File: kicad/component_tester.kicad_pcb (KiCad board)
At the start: 2 copper layers, 100.4 x 83 mm, 86 parts, among them IC201 MCP1640, IC202 ATmega328P-MMH, IC301 FT232RL, IC302 MAX1811, J301 0R-JUMPA, J302 0R-JUMPA, Q201 8 MHz, Q401 BSS138, Q402 BSS138, SW201 EVQ, T201 PMV65XP, T202 BSS84, T203 BSS123, T204 BC847, T301 BSS123, U401 VREG_SOT23-5, X201 MICRO-USB, X202 ISP

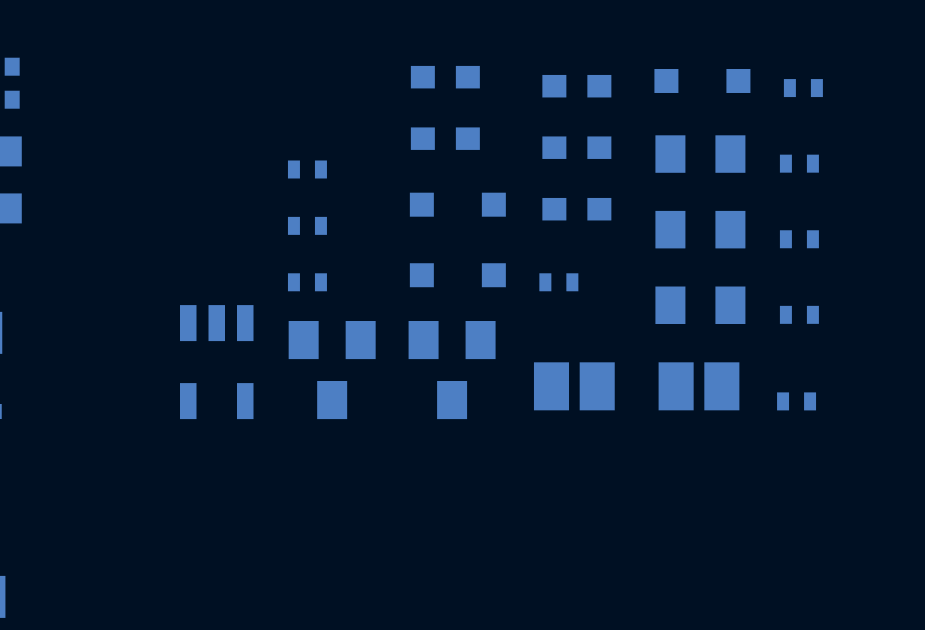
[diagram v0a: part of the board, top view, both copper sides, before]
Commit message: Remove unnecessary stuff from OLED circuitry
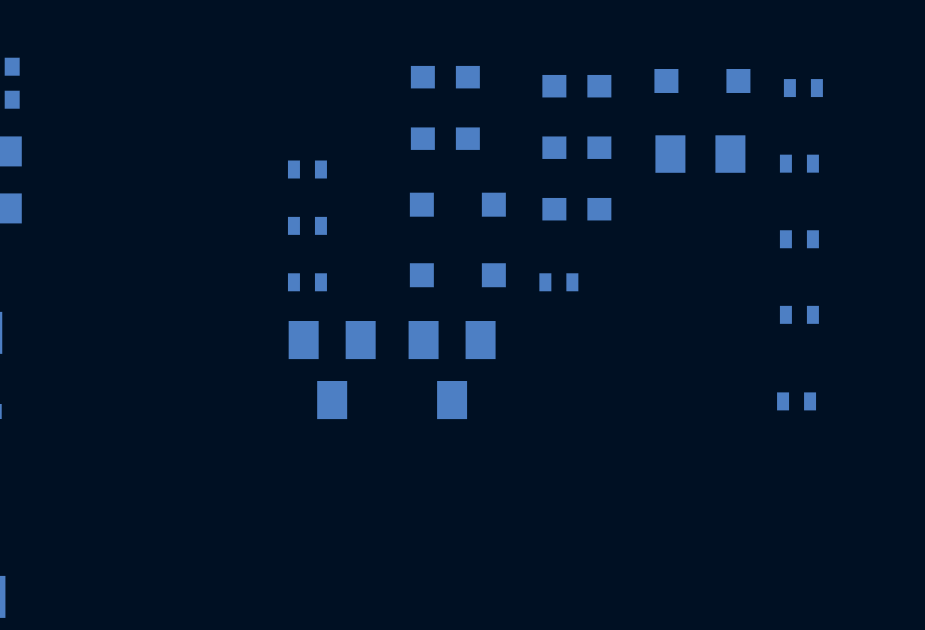
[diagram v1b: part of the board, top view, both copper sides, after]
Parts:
- removed C401, C402: 10uF, KiCad/Capacitors_SMD.pretty:C_0805
- removed SJ401, SJ402: SOLDERJUMPERREFLOW_NOPASTE, Adafruit 128x64 Mono OLED PCB v2:SOLDERJUMPER_REFLOW_NOPASTE
- removed U401: VREG_SOT23-5, Adafruit 128x64 Mono OLED PCB v2:SOT23-5
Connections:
- C407 pad 2: 3.3V -> +BATT
- C408 pad 2: 3.3V -> +BATT
- OLED1 pad 6: 3.3V -> +BATT
- OLED1 pad 9: 3.3V -> +BATT
- Q401 pad 1: 3.3V -> +BATT
- Q402 pad 1: 3.3V -> +BATT
- R401 pad 2: 3.3V -> +BATT
- R402 pad 2: 3.3V -> +BATT
- R403 pad 2: VIN -> +5V
- R404 pad 2: VIN -> +5V
- R405 pad 2: 3.3V -> +BATT
- R406 pad 2: 3.3V -> +BATT
- R407 pad 2: 3.3V -> +BATT

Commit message: Work on placement
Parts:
- moved R218 116.2 mm to (178.1, 111.6), turned to 90 degrees
- moved R217 110.9 mm to (177.3, 106.7)
- moved R214 108.1 mm to (179.1, 106.9)
- moved R215 107.4 mm to (178.3, 104.4)
- moved R216 106.7 mm to (176.0, 103.9)
- moved R219 96.0 mm to (179.1, 110.0), turned to 270 degrees
- moved C201 88.9 mm to (160.3, 105.4)
- moved IC201 67.2 mm to (160.5, 110.2), turned to 90 degrees
- moved R201 63.2 mm to (106.4, 96.3)
- moved T201 42.4 mm to (102.9, 96.0), turned to 270 degrees
- moved C204 1.78 mm to (166.5, 106.6)
- moved C205 1.78 mm to (166.4, 109.6)
- moved IC202 1.78 mm to (174.1, 108.1)
- moved Q201 1.78 mm to (169.1, 108.1)

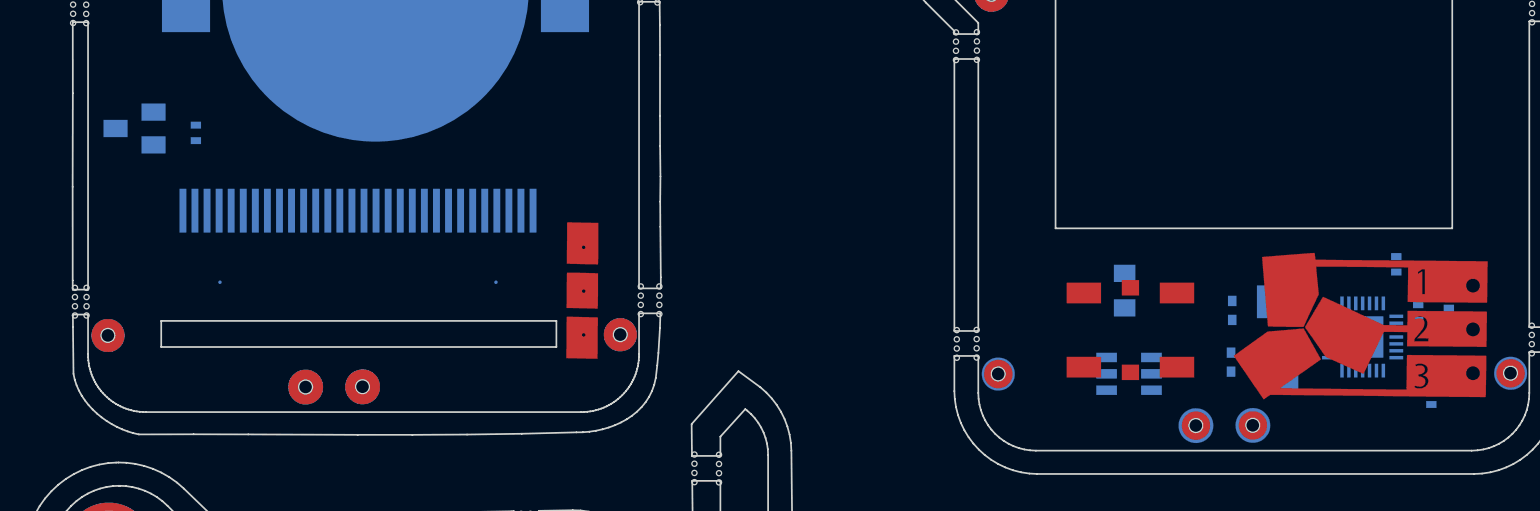
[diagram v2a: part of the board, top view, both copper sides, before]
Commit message: Add drawings of inner edges to help with layout
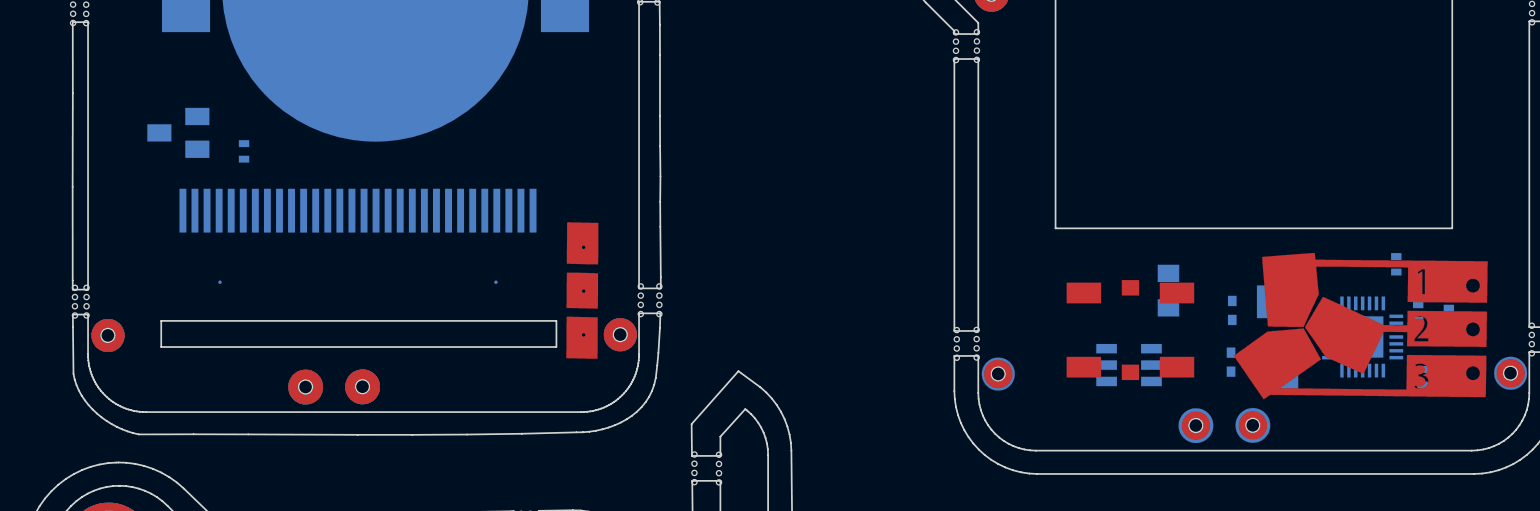
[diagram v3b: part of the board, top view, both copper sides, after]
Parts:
- moved R201 2.99 mm to (109.2, 97.3)
- moved T201 2.55 mm to (105.4, 96.3)
- moved C201 2.54 mm to (162.8, 105.4)
- moved R218 1.24 mm to (177.5, 110.4)
- moved IC201 0.51 mm to (160.5, 109.7)

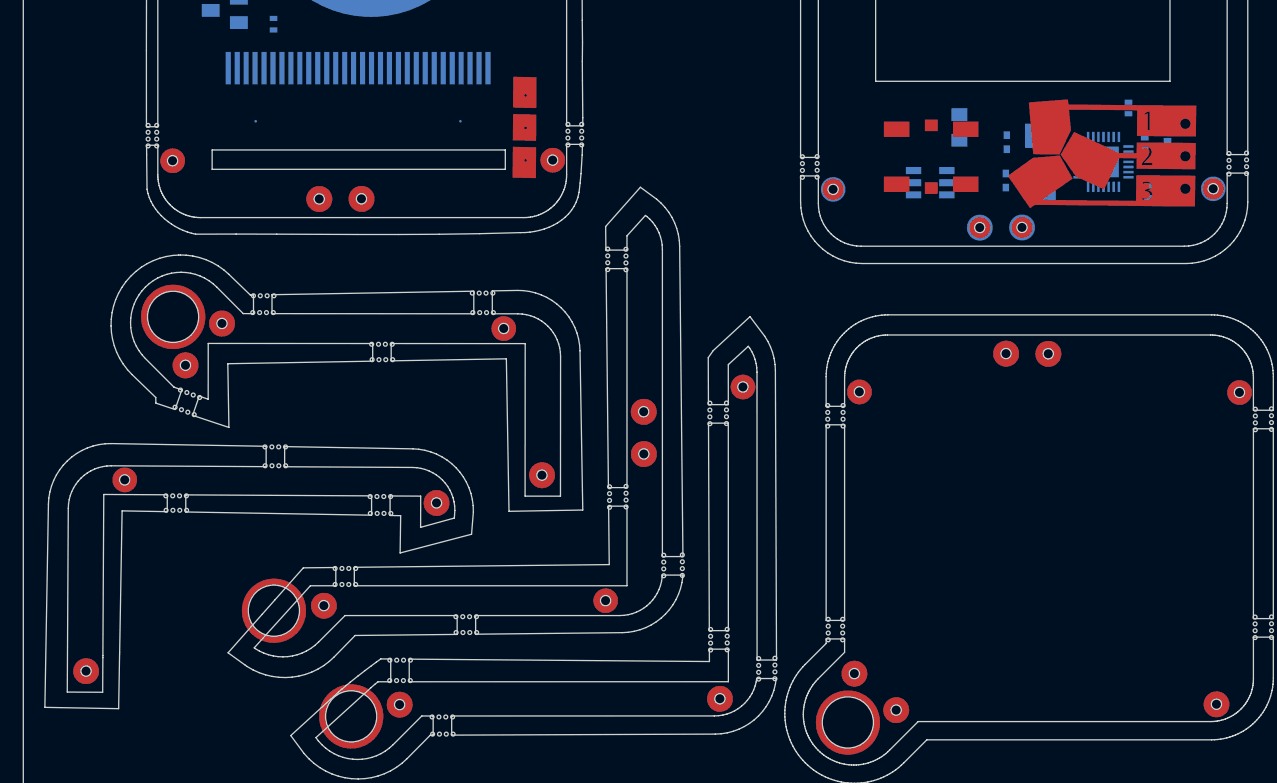
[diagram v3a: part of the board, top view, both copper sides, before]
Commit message: Adjust pads placement tonot interfere with screen
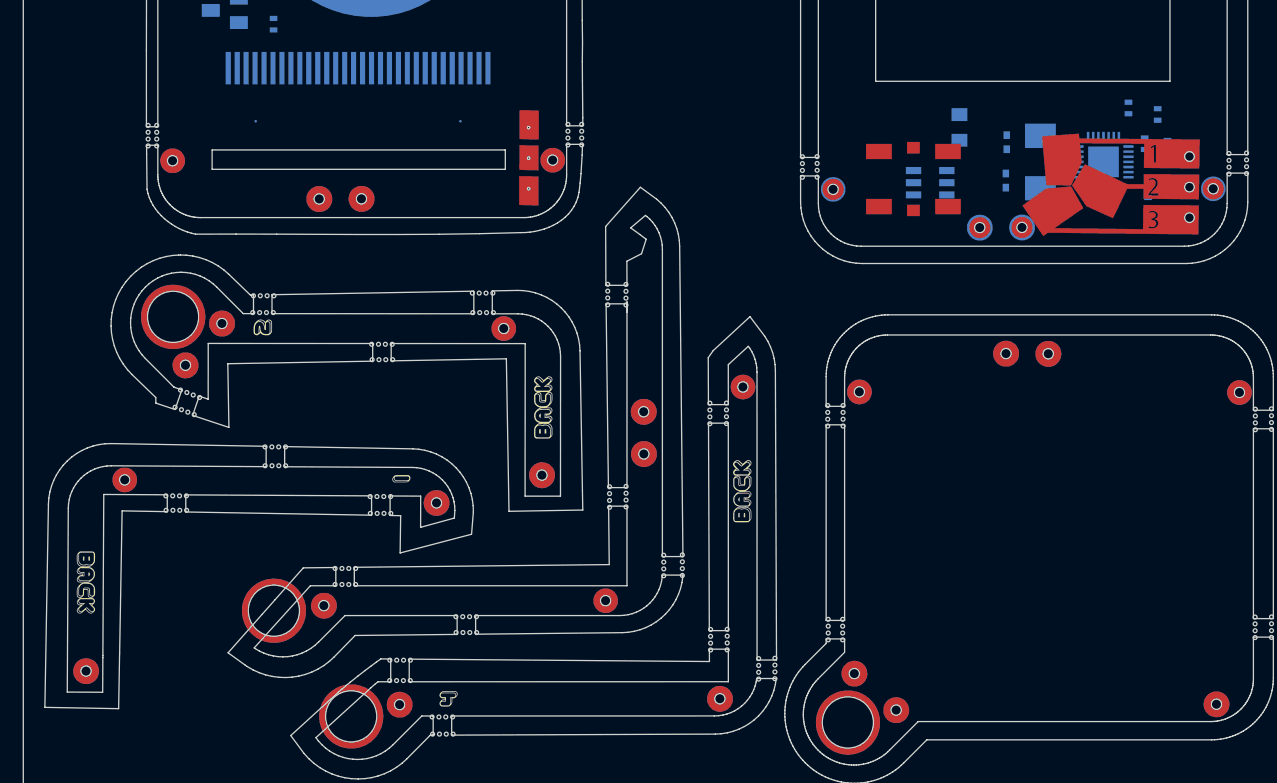
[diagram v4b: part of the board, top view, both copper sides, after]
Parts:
- moved DRAWING202 3.47 mm to (120.7, 101.6)
- moved DRAWING201 2.45 mm to (170.8, 103.7)
- moved SW201 2.23 mm to (159.2, 109.4)
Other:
- outline, holes or cut-outs redrawn

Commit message: Work on placing components
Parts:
- L201: value 4,7 uH -> 4.7uH; footprint component_tester:L1210 -> KiCad/Resistors_SMD.pretty:R_0603
- Q201: footprint KiCad/Crystals.pretty:Crystal_SMD_Abracon_ABM3-2pin_5.0x3.2mm -> mcous/kicad-lib/footprints/crystal.pretty:NDK-NX3225GA_xtal
- moved C202 96.6 mm to (170.8, 108.2), turned to 270 degrees
- moved C209 92.0 mm to (179.7, 106.3), turned to 270 degrees
- moved T202 90.0 mm to (166.6, 109.7)
- moved C208 76.3 mm to (179.8, 108.5), turned to 270 degrees
- moved R206 71.2 mm to (166.9, 108.3), turned to 270 degrees
- moved C210 69.7 mm to (179.8, 110.7), turned to 90 degrees
- moved L201 62.4 mm to (162.8, 105.3)
- moved D202 14.9 mm to (120.5, 68.2)
- moved Q201 12.4 mm to (156.8, 109.5), turned to 270 degrees
- moved C201 8.47 mm to (171.2, 104.2), turned to 0 degrees
- moved R216 3.64 mm to (177.4, 107.3), turned to 270 degrees
- moved R215 2.87 mm to (178.6, 107.2), turned to 270 degrees
- moved R214 2.73 mm to (177.4, 109.0)
- moved R217 2.64 mm to (178.6, 109.0)
- moved C204 2.06 mm to (164.5, 106.1)
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
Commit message: Switch back to 0201s and continue placing
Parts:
- C202, C204, C205, C206, C208, C209, C210, C211, C212, C213: footprint KiCad/Capacitors_SMD.pretty:C_0402 -> KiCad/Capacitors_SMD.pretty:C_0201
- R201, R202, R203, R204, R205, R206, R207, R208, R209, R210, R211, R212, R213, R214, R215, R216, R217, R218, R219, R401, R402, R403, R404, R405, R406, R407, R408, R409: footprint KiCad/Resistors_SMD.pretty:R_0402 -> KiCad/Resistors_SMD.pretty:R_0201
- moved C211 91.1 mm to (180.6, 108.8), turned to 180 degrees
- moved C212 89.0 mm to (179.1, 110.2), turned to 0 degrees
- moved C213 84.2 mm to (179.1, 107.0), turned to 180 degrees
- moved C204 7.83 mm to (156.7, 105.5)
- moved C201 6.90 mm to (169.6, 110.9), turned to 180 degrees
- moved R206 6.10 mm to (160.9, 107.0)
- moved C205 6.05 mm to (158.8, 107.0)
- moved R215 4.08 mm to (177.7, 111.2), turned to 180 degrees
- moved R219 3.84 mm to (177.7, 107.0), turned to 0 degrees
- moved C209 2.87 mm to (179.1, 109.1), turned to 0 degrees
- moved R214 2.81 mm to (179.1, 111.2), turned to 0 degrees
- moved R218 2.73 mm to (177.7, 108.1), turned to 0 degrees
- moved R216 1.92 mm to (177.7, 109.2), turned to 0 degrees
- moved R217 1.45 mm to (177.7, 110.2), turned to 0 degrees
- moved C202 1.15 mm to (170.8, 109.3)
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
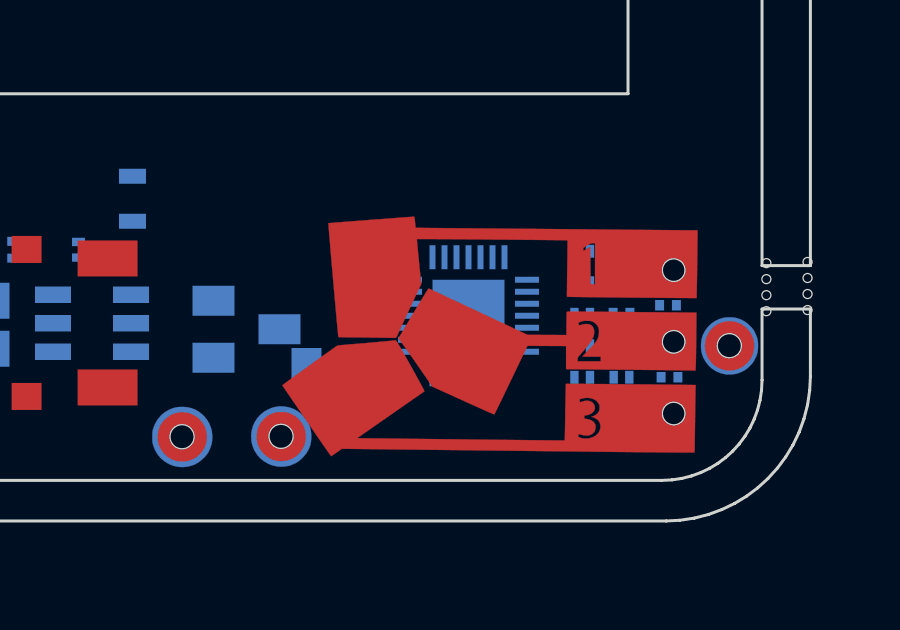
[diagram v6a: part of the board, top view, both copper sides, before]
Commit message: Set up design rules and test out routing a bit
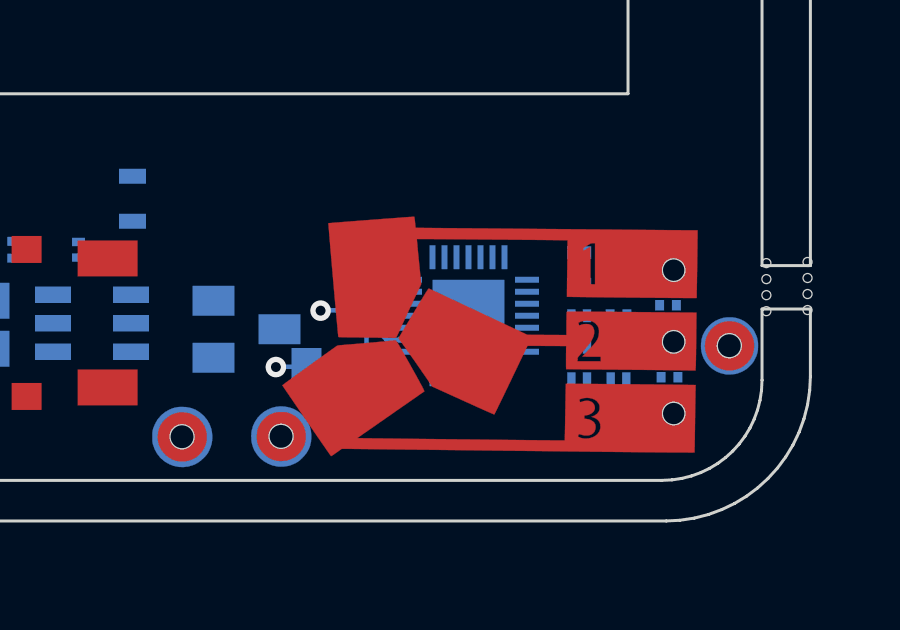
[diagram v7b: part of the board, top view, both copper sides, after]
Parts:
- moved R218 0.11 mm to (177.6, 108.2)
- moved C208 0.11 mm to (178.9, 108.1)
- moved C209 0.11 mm to (178.9, 109.2)
- moved C212 0.11 mm to (178.9, 110.2)
- moved C213 0.11 mm to (178.9, 107.1)
- moved R214 0.11 mm to (178.9, 111.3)
- moved R215 0.11 mm to (177.6, 111.3)
- moved R216 0.11 mm to (177.6, 109.2)
- moved R217 0.11 mm to (177.6, 110.2)
- moved R219 0.11 mm to (177.6, 107.1)
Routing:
- net GND: track 0.00 -> 2.81 mm, vias 0 -> 2
- net +5V: track 0.00 -> 2.80 mm
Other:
- copper layers 2 -> 4
- net class Default: trace_width 0.25 -> 0.1524; via_dia 0.8 -> 0.6858; via_drill 0.4 -> 0.3302
- rule trace_min: 0.2 -> 0.1524
- rule via_min_drill: 0.3 -> 0.254
- rule via_min_size: 0.4 -> 0.508
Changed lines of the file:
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@@
     (thickness 1.6)
     (drawings 7)
-    (tracks 0)
+    (tracks 10)
     (zones 0)
     (modules 81)
@@
   (page A4)
   (layers
-    (0 Top signal hide)
+    (0 Top signal)
+    (1 In1.Cu signal)
+    (2 In2.Cu signal)
     (31 Bottom signal)
-    (32 B.Adhes user hide)
-    (33 F.Adhes user hide)
+    (32 B.Adhes user)
+    (33 F.Adhes user)
     (34 B.Paste user)
-    (35 F.Paste user hide)
+    (35 F.Paste user)
     (36 B.SilkS user)
-    (37 F.SilkS user hide)
+    (37 F.SilkS user)
     (38 B.Mask user)
-    (39 F.Mask user hide)
+    (39 F.Mask user)
     (40 Dwgs.User user)
-    (41 Cmts.User user hide)
-    (42 Eco1.User user hide)
-    (43 Eco2.User user hide)
+    (41 Cmts.User user)
+    (42 Eco1.User user)
+    (43 Eco2.User user)
     (44 Edge.Cuts user)
-    (45 Margin user hide)
+    (45 Margin user)
     (46 B.CrtYd user)
-    (47 F.CrtYd user hide)
+    (47 F.CrtYd user)
     (48 B.Fab user)
-    (49 F.Fab user hide)
+    (49 F.Fab user)
   )
   (setup
-    (last_trace_width 0.25)
+    (last_trace_width 0.1524)
     (trace_clearance 0.1524)
     (zone_clearance 0)
     (zone_45_only no)
-    (trace_min 0.2)
+    (trace_min 0.1524)
     (segment_width 0.2)
     (edge_width 0.15)
-    (via_size 0.8)
-    (via_drill 0.4)
-    (via_min_size 0.4)
-    (via_min_drill 0.3)
-    (uvia_size 0.3)
-    (uvia_drill 0.1)
+    (via_size 0.6858)
+    (via_drill 0.3302)
+    (via_min_size 0.508)
+    (via_min_drill 0.254)
+    (uvia_size 0.6858)
+    (uvia_drill 0.3302)
     (uvias_allowed no)
     (uvia_min_size 0.2)
@@
   (net_class Default "This is the default net class."
     (clearance 0.1524)
-    (trace_width 0.25)
-    (via_dia 0.8)
-    (via_drill 0.4)
-    (uvia_dia 0.3)
-    (uvia_drill 0.1)
+    (trace_width 0.1524)
+    (via_dia 0.6858)
+    (via_drill 0.3302)
+    (uvia_dia 0.6858)
+    (uvia_drill 0.3302)
     (add_net +5V)
     (add_net +BATT)
@@
   )
   (module KiCad/Capacitors_SMD.pretty:C_0201 (layer Bottom)
-    (at 179.05 108.06)
+    (at 178.95 108.11)
     (descr "Capacitor SMD 0201, reflow soldering, AVX (see smccp.pdf)")
     (tags "capacitor 0201")
@@
   )
   (module KiCad/Capacitors_SMD.pretty:C_0201 (layer Bottom)
-    (at 179.05 109.11)
+    (at 178.95 109.16)
     (descr "Capacitor SMD 0201, reflow soldering, AVX (see smccp.pdf)")
     (tags "capacitor 0201")
@@
   )
   (module KiCad/Capacitors_SMD.pretty:C_0201 (layer Bottom)
-    (at 179.05 110.16)
+    (at 178.95 110.21)
     (descr "Capacitor SMD 0201, reflow soldering, AVX (see smccp.pdf)")
     (tags "capacitor 0201")
@@
   )
   (module KiCad/Capacitors_SMD.pretty:C_0201 (layer Bottom)
-    (at 179.05 107.01 180)
+    (at 178.95 107.06 180)
     (descr "Capacitor SMD 0201, reflow soldering, AVX (see smccp.pdf)")
     (tags "capacitor 0201")
@@
   )
   (module KiCad/Resistors_SMD.pretty:R_0201 (layer Bottom)
-    (at 179.05 111.25)
+    (at 178.95 111.3)
     (descr "Resistor SMD 0201, reflow soldering, Vishay (see crcw0201e3.pdf)")
     (tags "resistor 0201")
@@
   )
   (module KiCad/Resistors_SMD.pretty:R_0201 (layer Bottom)
-    (at 177.74 107.05)
+    (at 177.64 107.1)
     (descr "Resistor SMD 0201, reflow soldering, Vishay (see crcw0201e3.pdf)")
     (tags "resistor 0201")
@@
   )
   (module KiCad/Resistors_SMD.pretty:R_0201 (layer Bottom)
-    (at 177.74 108.1)
+    (at 177.64 108.15)
     (descr "Resistor SMD 0201, reflow soldering, Vishay (see crcw0201e3.pdf)")
     (tags "resistor 0201")
@@
   )
   (module KiCad/Resistors_SMD.pretty:R_0201 (layer Bottom)
-    (at 177.74 110.2)
+    (at 177.64 110.25)
     (descr "Resistor SMD 0201, reflow soldering, Vishay (see crcw0201e3.pdf)")
     (tags "resistor 0201")
@@
   )
   (module KiCad/Resistors_SMD.pretty:R_0201 (layer Bottom)
-    (at 177.74 109.15)
+    (at 177.64 109.2)
     (descr "Resistor SMD 0201, reflow soldering, Vishay (see crcw0201e3.pdf)")
     (tags "resistor 0201")
@@
   )
   (module KiCad/Resistors_SMD.pretty:R_0201 (layer Bottom)
-    (at 177.74 111.25 180)
+    (at 177.64 111.3 180)
     (descr "Resistor SMD 0201, reflow soldering, Vishay (see crcw0201e3.pdf)")
     (tags "resistor 0201")
@@
     (effects (font (size 1.35128 1.35128) (thickness 0.113792)) (justify right top))
   )
+  (via (at 167.53 110.91) (size 0.6858) (drill 0.3302) (layers Top Bottom) (net 1))
+  (segment (start 168.55 110.9) (end 167.54 110.9) (width 0.1524) (layer Bottom) (net 1))
+  (segment (start 167.54 110.9) (end 167.53 110.91) (width 0.1524) (layer Bottom) (net 1))
+  (via (at 169.02 109.03) (size 0.6858) (drill 0.3302) (layers Top Bottom) (net 1))
+  (segment (start 170.8 109.02) (end 169.03 109.02) (width 0.1524) (layer Bottom) (net 1))
+  (segment (start 169.03 109.02) (end 169.02 109.03) (width 0.1524) (layer Bottom) (net 1))
+  (segment (start 170.55 109.83) (end 170.8 109.58) (width 0.1524) (layer Bottom) (net 8))
+  (segment (start 170.55 110.9) (end 170.55 109.83) (width 0.1524) (layer Bottom) (net 8))
+  (segment (start 171.22 110) (end 172 110) (width 0.1524) (layer Bottom) (net 8))
+  (segment (start 170.8 109.58) (end 171.22 110) (width 0.1524) (layer Bottom) (net 8))
 )
